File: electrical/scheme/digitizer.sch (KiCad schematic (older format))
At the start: 149 parts, among them P1 mode, P10 in-2, P11 in-3, P12 in-1, P13 USB_B, P2 ~rst~, P3 ext, P4 trig, P5 trig-mode, P6 swd, P7 out-0, P8 out-1, P9 in-0, U1 AD8672, U10 crystal-4pin, U100 AD8672, U101 AD8672, U11 CP2102, U12 adr4533, U13 BAT54S, U14 adr4533, U15 ADT7410, U16 MCP1703T-3302E/CB, U17 AD7683, U18 NCP3063, U19 ADG5204, U2 AD8672, U20 NCP3063, U3 AD8672

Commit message: a
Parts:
- added R77, R78: 1k 5%, Resistors_SMD:R_0805_HandSoldering, symbol R
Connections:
- wire segments 542 -> 544
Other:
- moved on the sheet: P7, P8
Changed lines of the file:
@@
 L BNC P7
 U 1 1 55AB2116
-P 24400 7650
-F 0 "P7" H 24410 7770 50  0000 C CNN
-F 1 "out-0" V 24510 7590 50  0000 C CNN
-F 2 "Sockets_BNC:BNC_Socket_TYCO-AMP_LargePads" H 24400 7650 60  0001 C CNN
-F 3 "" H 24400 7650 60  0000 C CNN
-	1    24400 7650
+P 24900 7650
+F 0 "P7" H 24910 7770 50  0000 C CNN
+F 1 "out-0" V 25010 7590 50  0000 C CNN
+F 2 "Sockets_BNC:BNC_Socket_TYCO-AMP_LargePads" H 24900 7650 60  0001 C CNN
+F 3 "" H 24900 7650 60  0000 C CNN
+	1    24900 7650
 	1    0    0    -1
 $EndComp
@@
 L GNDA #PWR075
 U 1 1 55AB5E7E
-P 24400 7950
-F 0 "#PWR075" H 24400 7700 50  0001 C CNN
-F 1 "GNDA" H 24400 7800 50  0000 C CNN
-F 2 "" H 24400 7950 60  0000 C CNN
-F 3 "" H 24400 7950 60  0000 C CNN
-	1    24400 7950
+P 24900 7950
+F 0 "#PWR075" H 24900 7700 50  0001 C CNN
+F 1 "GNDA" H 24900 7800 50  0000 C CNN
+F 2 "" H 24900 7950 60  0000 C CNN
+F 3 "" H 24900 7950 60  0000 C CNN
+	1    24900 7950
 	1    0    0    -1
 $EndComp
@@
 L BNC P8
 U 1 1 55ABA9EF
-P 24450 11850
-F 0 "P8" H 24460 11970 50  0000 C CNN
-F 1 "out-1" V 24560 11790 50  0000 C CNN
-F 2 "Sockets_BNC:BNC_Socket_TYCO-AMP_LargePads" H 24450 11850 60  0001 C CNN
-F 3 "" H 24450 11850 60  0000 C CNN
-	1    24450 11850
+P 24950 11850
+F 0 "P8" H 24960 11970 50  0000 C CNN
+F 1 "out-1" V 25060 11790 50  0000 C CNN
+F 2 "Sockets_BNC:BNC_Socket_TYCO-AMP_LargePads" H 24950 11850 60  0001 C CNN
+F 3 "" H 24950 11850 60  0000 C CNN
+	1    24950 11850
 	1    0    0    -1
 $EndComp
@@
 L GNDA #PWR076
 U 1 1 55ABA9F6
-P 24450 12150
-F 0 "#PWR076" H 24450 11900 50  0001 C CNN
-F 1 "GNDA" H 24450 12000 50  0000 C CNN
-F 2 "" H 24450 12150 60  0000 C CNN
-F 3 "" H 24450 12150 60  0000 C CNN
-	1    24450 12150
+P 24950 12150
+F 0 "#PWR076" H 24950 11900 50  0001 C CNN
+F 1 "GNDA" H 24950 12000 50  0000 C CNN
+F 2 "" H 24950 12150 60  0000 C CNN
+F 3 "" H 24950 12150 60  0000 C CNN
+	1    24950 12150
 	1    0    0    -1
 $EndComp
@@
 	1700 12200 1700 12450
 Wire Wire Line
-	24400 7850 24400 7950
-Wire Wire Line
-	24450 12050 24450 12150
+	24900 7850 24900 7950
+Wire Wire Line
+	24950 12050 24950 12150
 Wire Wire Line
 	9150 3000 10000 3000
@@
 Text Label 11500 15750 0    60   ~ 0
 i2c1-sda
+$Comp
+L R R77
+U 1 1 55B37111
+P 24400 7650
+F 0 "R77" V 24480 7650 50  0000 C CNN
+F 1 "1k 5%" V 24400 7650 50  0000 C CNN
+F 2 "Resistors_SMD:R_0805_HandSoldering" V 24330 7650 30  0001 C CNN
+F 3 "" H 24400 7650 30  0000 C CNN
+	1    24400 7650
+	0    -1   -1   0
+$EndComp
+Wire Wire Line
+	24750 7650 24550 7650
+$Comp
+L R R78
+U 1 1 55B3C1AC
+P 24450 11850
+F 0 "R78" V 24530 11850 50  0000 C CNN
+F 1 "1k 5%" V 24450 11850 50  0000 C CNN
+F 2 "Resistors_SMD:R_0805_HandSoldering" V 24380 11850 30  0001 C CNN
+F 3 "" H 24450 11850 30  0000 C CNN
+	1    24450 11850
+	0    -1   -1   0
+$EndComp
+Wire Wire Line
+	24800 11850 24600 11850
 $EndSCHEMATC

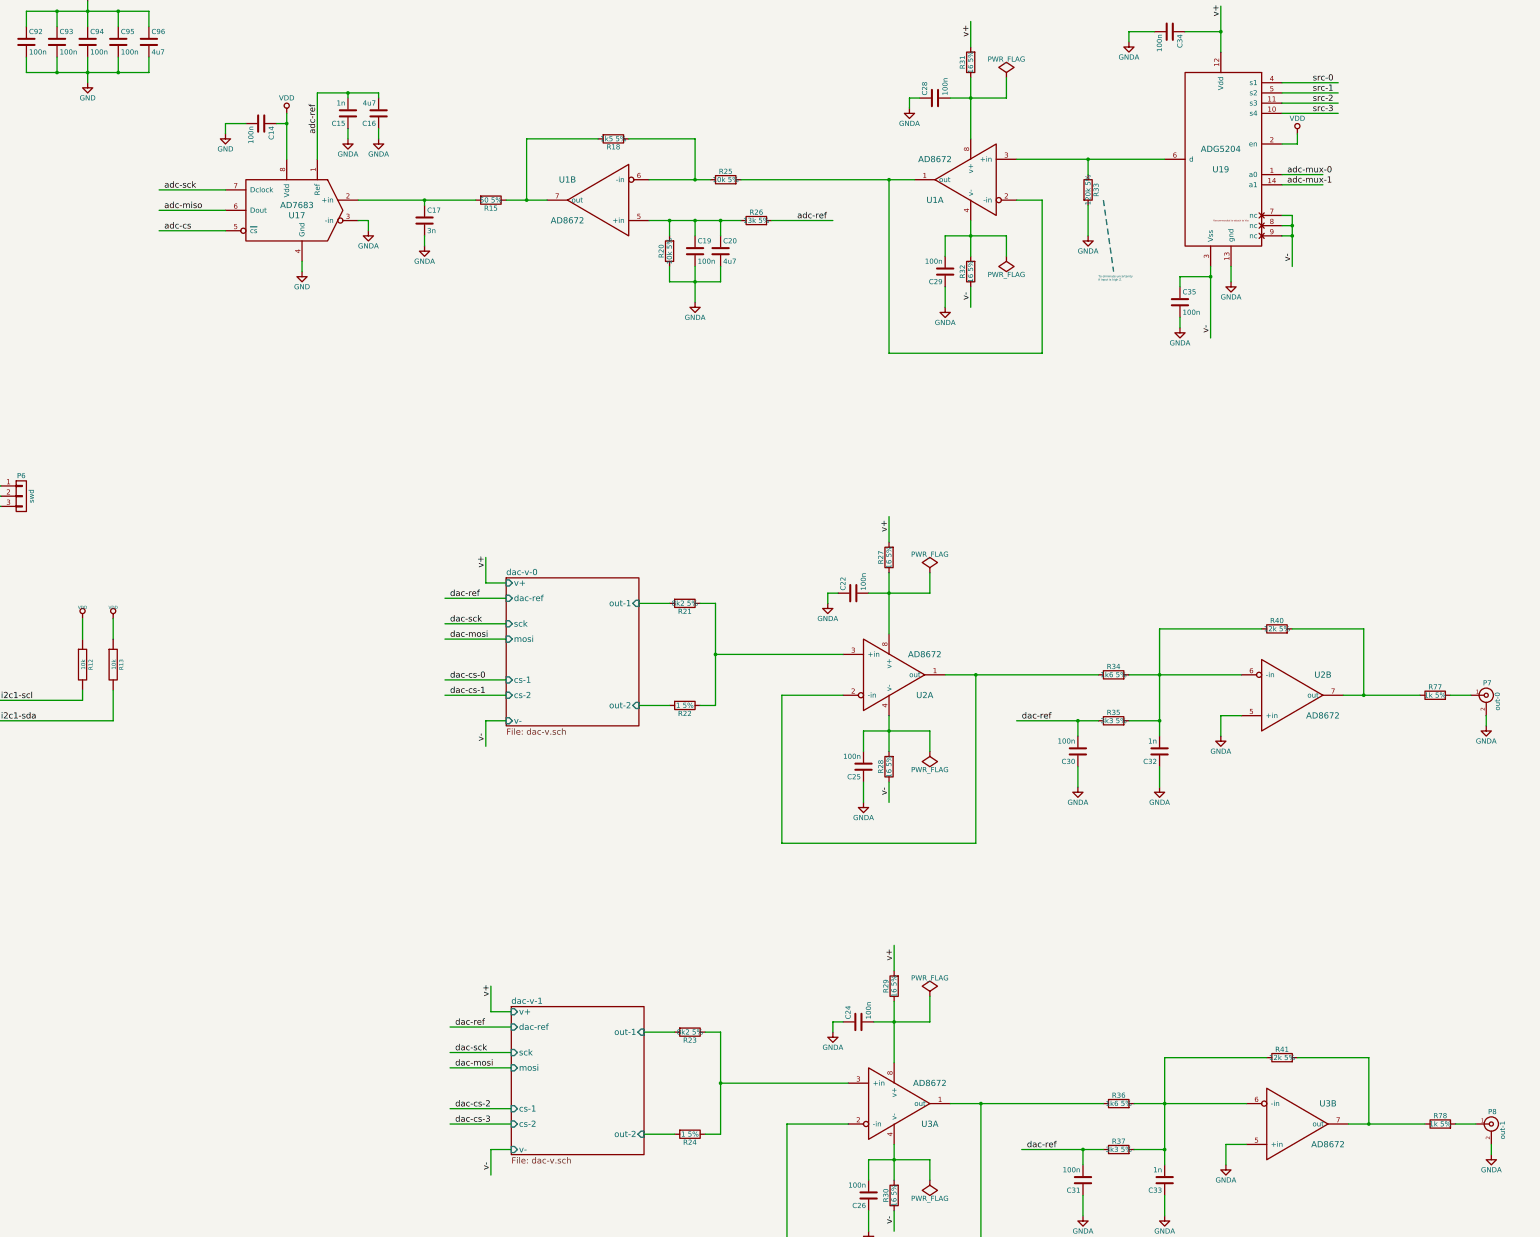
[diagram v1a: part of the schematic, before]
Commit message: Added capacitors for making opamp driving capacitive load stable.
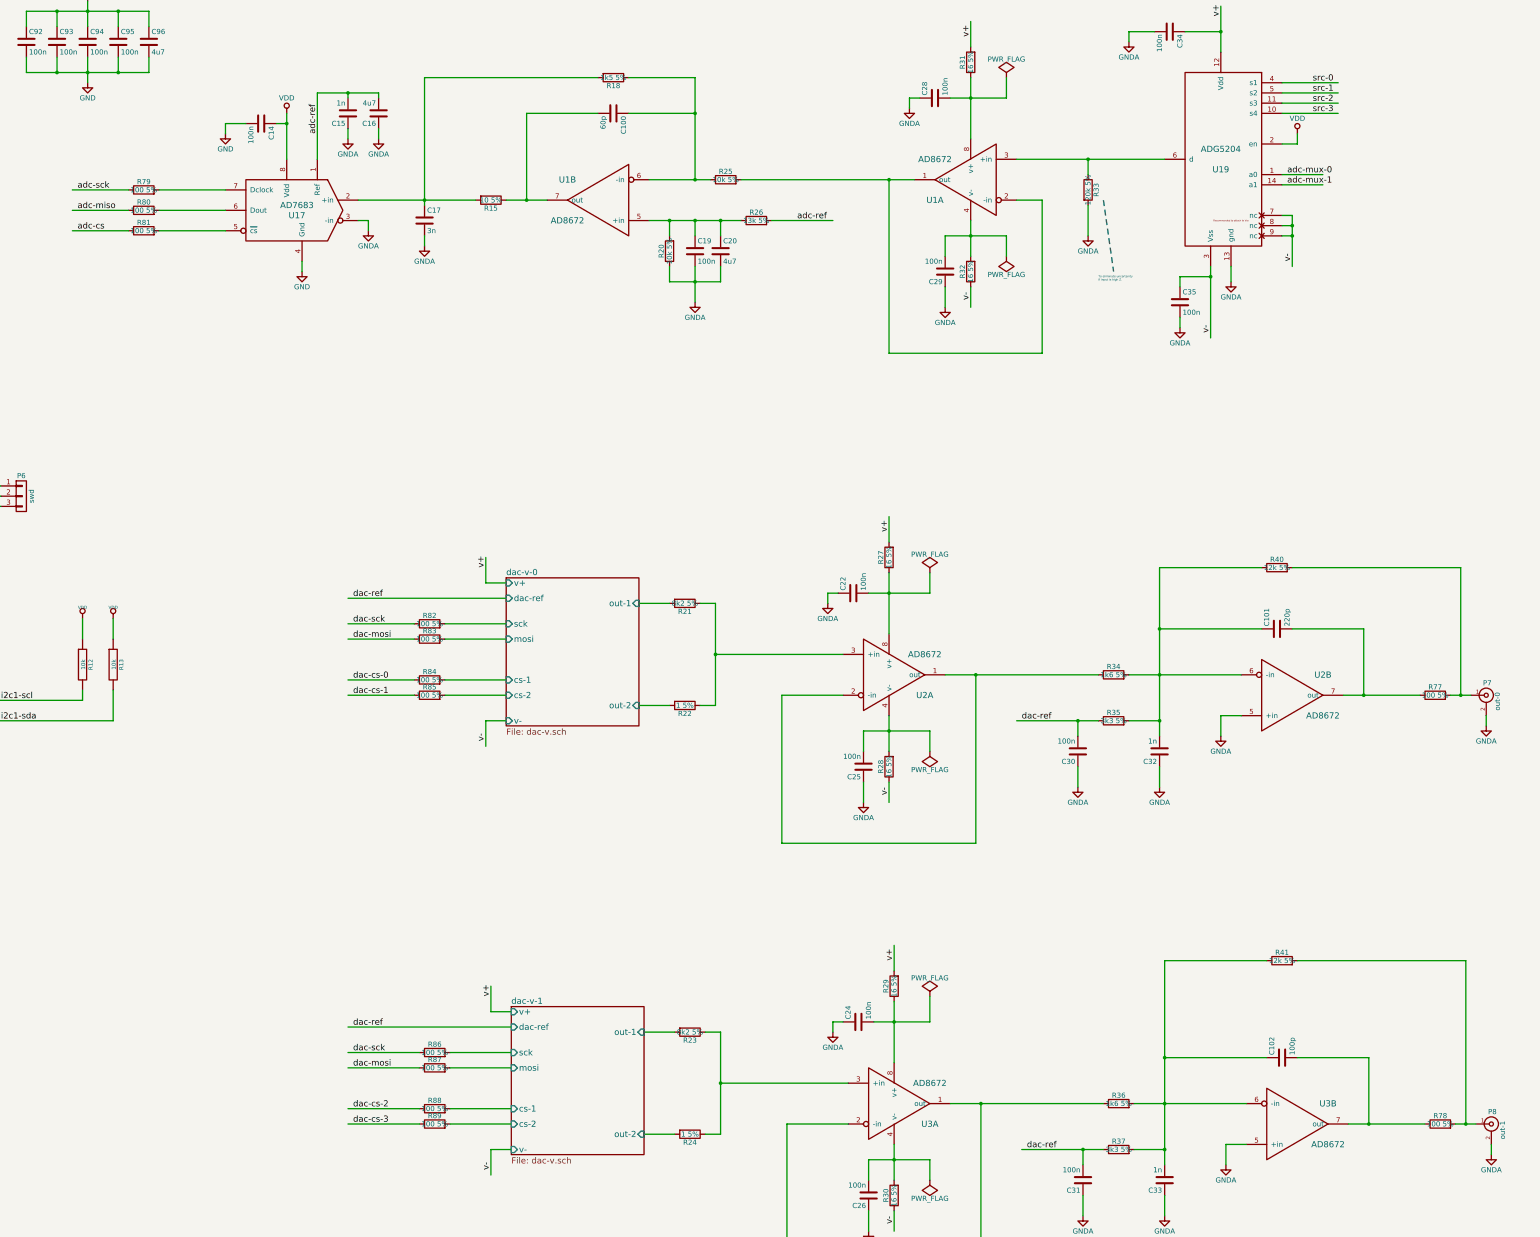
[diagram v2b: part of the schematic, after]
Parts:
- added C100: 60p, Capacitors_SMD:C_0805_HandSoldering, symbol C
- added C101: 220p, Capacitors_SMD:C_0805_HandSoldering, symbol C
- added C102: 100p, Capacitors_SMD:C_0805_HandSoldering, symbol C
- added R79, R80, R81, R82, R83, R84, R85, R86, R87, R88, R89: 100 5%, Resistors_SMD:R_0805_HandSoldering, symbol R
- R15: value 50 5% -> 10 5%
- R77, R78: value 1k 5% -> 100 5%
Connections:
- wire segments 544 -> 563
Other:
- moved on the sheet: R18, R40, R41

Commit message: a
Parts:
- added R90, R91, R92, R93: 1k 5%, Resistors_SMD:R_0805_HandSoldering, symbol R
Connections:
- wire segments 563 -> 567
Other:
- moved on the sheet: P10, P11, P12, P9
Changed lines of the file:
@@
 L BNC P9
 U 1 1 559CB400
-P 30950 3300
-F 0 "P9" H 30960 3420 50  0000 C CNN
-F 1 "in-0" V 31060 3240 50  0000 C CNN
-F 2 "Sockets_BNC:BNC_Socket_TYCO-AMP_LargePads" H 30950 3300 60  0001 C CNN
-F 3 "" H 30950 3300 60  0000 C CNN
-	1    30950 3300
+P 31450 3300
+F 0 "P9" H 31460 3420 50  0000 C CNN
+F 1 "in-0" V 31560 3240 50  0000 C CNN
+F 2 "Sockets_BNC:BNC_Socket_TYCO-AMP_LargePads" H 31450 3300 60  0001 C CNN
+F 3 "" H 31450 3300 60  0000 C CNN
+	1    31450 3300
 	1    0    0    -1
 $EndComp
@@
 L GNDA #PWR058
 U 1 1 559CD9D7
-P 30950 3600
-F 0 "#PWR058" H 30950 3350 50  0001 C CNN
-F 1 "GNDA" H 30950 3450 50  0000 C CNN
-F 2 "" H 30950 3600 60  0000 C CNN
-F 3 "" H 30950 3600 60  0000 C CNN
-	1    30950 3600
+P 31450 3600
+F 0 "#PWR058" H 31450 3350 50  0001 C CNN
+F 1 "GNDA" H 31450 3450 50  0000 C CNN
+F 2 "" H 31450 3600 60  0000 C CNN
+F 3 "" H 31450 3600 60  0000 C CNN
+	1    31450 3600
 	1    0    0    -1
 $EndComp
@@
 L BNC P10
 U 1 1 55BF1FCC
-P 30900 9350
-F 0 "P10" H 30910 9470 50  0000 C CNN
-F 1 "in-2" V 31010 9290 50  0000 C CNN
-F 2 "Sockets_BNC:BNC_Socket_TYCO-AMP_LargePads" H 30900 9350 60  0001 C CNN
-F 3 "" H 30900 9350 60  0000 C CNN
-	1    30900 9350
+P 31400 9350
+F 0 "P10" H 31410 9470 50  0000 C CNN
+F 1 "in-2" V 31510 9290 50  0000 C CNN
+F 2 "Sockets_BNC:BNC_Socket_TYCO-AMP_LargePads" H 31400 9350 60  0001 C CNN
+F 3 "" H 31400 9350 60  0000 C CNN
+	1    31400 9350
 	1    0    0    -1
 $EndComp
@@
 L GNDA #PWR0100
 U 1 1 55BF1FD3
-P 30900 9650
-F 0 "#PWR0100" H 30900 9400 50  0001 C CNN
-F 1 "GNDA" H 30900 9500 50  0000 C CNN
-F 2 "" H 30900 9650 60  0000 C CNN
-F 3 "" H 30900 9650 60  0000 C CNN
-	1    30900 9650
+P 31400 9650
+F 0 "#PWR0100" H 31400 9400 50  0001 C CNN
+F 1 "GNDA" H 31400 9500 50  0000 C CNN
+F 2 "" H 31400 9650 60  0000 C CNN
+F 3 "" H 31400 9650 60  0000 C CNN
+	1    31400 9650
 	1    0    0    -1
 $EndComp
@@
 L BNC P12
 U 1 1 55BF7CDF
-P 30950 5950
-F 0 "P12" H 30960 6070 50  0000 C CNN
-F 1 "in-1" V 31060 5890 50  0000 C CNN
-F 2 "Sockets_BNC:BNC_Socket_TYCO-AMP_LargePads" H 30950 5950 60  0001 C CNN
-F 3 "" H 30950 5950 60  0000 C CNN
-	1    30950 5950
+P 31450 5950
+F 0 "P12" H 31460 6070 50  0000 C CNN
+F 1 "in-1" V 31560 5890 50  0000 C CNN
+F 2 "Sockets_BNC:BNC_Socket_TYCO-AMP_LargePads" H 31450 5950 60  0001 C CNN
+F 3 "" H 31450 5950 60  0000 C CNN
+	1    31450 5950
 	1    0    0    -1
 $EndComp
@@
 L GNDA #PWR0105
 U 1 1 55BF7CE6
-P 30950 6250
-F 0 "#PWR0105" H 30950 6000 50  0001 C CNN
-F 1 "GNDA" H 30950 6100 50  0000 C CNN
-F 2 "" H 30950 6250 60  0000 C CNN
-F 3 "" H 30950 6250 60  0000 C CNN
-	1    30950 6250
+P 31450 6250
+F 0 "#PWR0105" H 31450 6000 50  0001 C CNN
+F 1 "GNDA" H 31450 6100 50  0000 C CNN
+F 2 "" H 31450 6250 60  0000 C CNN
+F 3 "" H 31450 6250 60  0000 C CNN
+	1    31450 6250
 	1    0    0    -1
 $EndComp
@@
 L BNC P11
 U 1 1 55BFAAD0
-P 30900 12150
-F 0 "P11" H 30910 12270 50  0000 C CNN
-F 1 "in-3" V 31010 12090 50  0000 C CNN
-F 2 "Sockets_BNC:BNC_Socket_TYCO-AMP_LargePads" H 30900 12150 60  0001 C CNN
-F 3 "" H 30900 12150 60  0000 C CNN
-	1    30900 12150
+P 31400 12150
+F 0 "P11" H 31410 12270 50  0000 C CNN
+F 1 "in-3" V 31510 12090 50  0000 C CNN
+F 2 "Sockets_BNC:BNC_Socket_TYCO-AMP_LargePads" H 31400 12150 60  0001 C CNN
+F 3 "" H 31400 12150 60  0000 C CNN
+	1    31400 12150
 	1    0    0    -1
 $EndComp
@@
 L GNDA #PWR0106
 U 1 1 55BFAAD7
-P 30900 12450
-F 0 "#PWR0106" H 30900 12200 50  0001 C CNN
-F 1 "GNDA" H 30900 12300 50  0000 C CNN
-F 2 "" H 30900 12450 60  0000 C CNN
-F 3 "" H 30900 12450 60  0000 C CNN
-	1    30900 12450
+P 31400 12450
+F 0 "#PWR0106" H 31400 12200 50  0001 C CNN
+F 1 "GNDA" H 31400 12300 50  0000 C CNN
+F 2 "" H 31400 12450 60  0000 C CNN
+F 3 "" H 31400 12450 60  0000 C CNN
+	1    31400 12450
 	1    0    0    -1
 $EndComp
@@
 	21150 2800 21250 3500
 Wire Wire Line
-	30950 3500 30950 3600
+	31450 3500 31450 3600
 Wire Wire Line
 	9150 15150 9850 15150
@@
 	28900 9150 29400 9150
 Wire Wire Line
-	30900 9550 30900 9650
+	31400 9550 31400 9650
 Wire Wire Line
 	30400 9350 30750 9350
@@
 Connection ~ 29300 5750
 Wire Wire Line
-	30950 6150 30950 6250
+	31450 6150 31450 6250
 Wire Wire Line
 	29350 11950 28900 11950
@@
 Connection ~ 29250 11950
 Wire Wire Line
-	30900 12350 30900 12450
+	31400 12350 31400 12450
 Wire Wire Line
 	5700 20850 6500 20850
@@
 	15500 1950 15500 2800
 Connection ~ 15500 2800
+$Comp
+L R R92
+U 1 1 55BD770F
+P 30950 3300
+F 0 "R92" V 31030 3300 50  0000 C CNN
+F 1 "1k 5%" V 30950 3300 50  0000 C CNN
+F 2 "Resistors_SMD:R_0805_HandSoldering" V 30880 3300 30  0001 C CNN
+F 3 "" H 30950 3300 30  0000 C CNN
+	1    30950 3300
+	0    1    1    0
+$EndComp
+Wire Wire Line
+	31100 3300 31300 3300
+$Comp
+L R R93
+U 1 1 55BDE631
+P 30950 5950
+F 0 "R93" V 31030 5950 50  0000 C CNN
+F 1 "1k 5%" V 30950 5950 50  0000 C CNN
+F 2 "Resistors_SMD:R_0805_HandSoldering" V 30880 5950 30  0001 C CNN
+F 3 "" H 30950 5950 30  0000 C CNN
+	1    30950 5950
+	0    1    1    0
+$EndComp
+Wire Wire Line
+	31100 5950 31300 5950
+$Comp
+L R R90
+U 1 1 55BE0CA7
+P 30900 9350
+F 0 "R90" V 30980 9350 50  0000 C CNN
+F 1 "1k 5%" V 30900 9350 50  0000 C CNN
+F 2 "Resistors_SMD:R_0805_HandSoldering" V 30830 9350 30  0001 C CNN
+F 3 "" H 30900 9350 30  0000 C CNN
+	1    30900 9350
+	0    1    1    0
+$EndComp
+Wire Wire Line
+	31250 9350 31050 9350
+$Comp
+L R R91
+U 1 1 55BE6200
+P 30900 12150
+F 0 "R91" V 30980 12150 50  0000 C CNN
+F 1 "1k 5%" V 30900 12150 50  0000 C CNN
+F 2 "Resistors_SMD:R_0805_HandSoldering" V 30830 12150 30  0001 C CNN
+F 3 "" H 30900 12150 30  0000 C CNN
+	1    30900 12150
+	0    1    1    0
+$EndComp
+Wire Wire Line
+	31050 12150 31250 12150
 $EndSCHEMATC

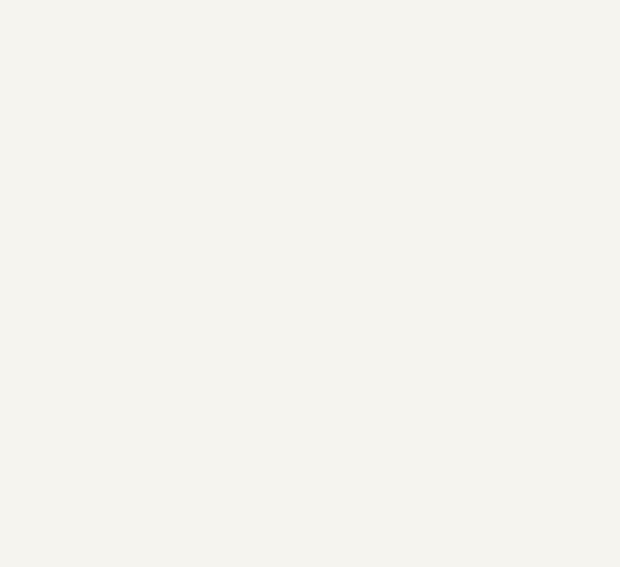
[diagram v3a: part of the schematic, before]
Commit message: Inserted holding screw holes.
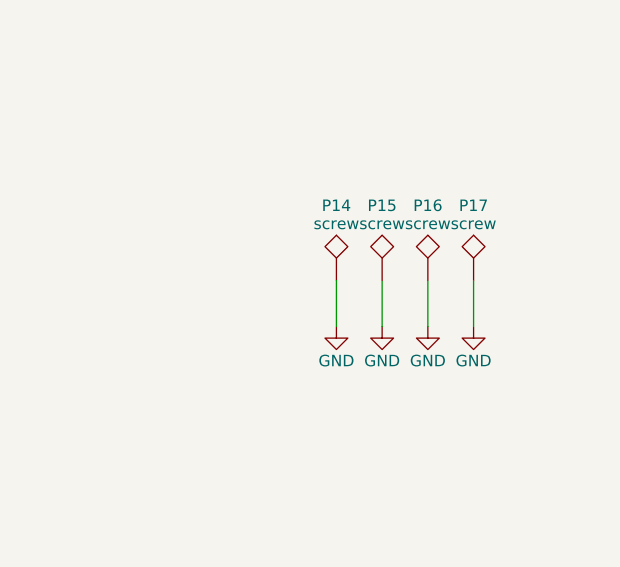
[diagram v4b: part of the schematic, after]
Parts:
- added P14, P15, P16, P17: screw, Divers:douille_4mm, symbol TST
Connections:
- wire segments 567 -> 571
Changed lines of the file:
@@
 Wire Wire Line
 	31050 12150 31250 12150
+$Comp
+L TST P14
+U 1 1 55C19FBA
+P 30450 15350
+F 0 "P14" H 30450 15650 50  0000 C BNN
+F 1 "screw" H 30450 15600 50  0000 C CNN
+F 2 "Divers:douille_4mm" H 30450 15350 60  0001 C CNN
+F 3 "" H 30450 15350 60  0000 C CNN
+	1    30450 15350
+	1    0    0    -1
+$EndComp
+Wire Wire Line
+	30450 15350 30450 15550
+$Comp
+L GND #PWR0131
+U 1 1 55C1E9F0
+P 30450 15550
+F 0 "#PWR0131" H 30450 15300 50  0001 C CNN
+F 1 "GND" H 30450 15400 50  0000 C CNN
+F 2 "" H 30450 15550 60  0000 C CNN
+F 3 "" H 30450 15550 60  0000 C CNN
+	1    30450 15550
+	1    0    0    -1
+$EndComp
+$Comp
+L TST P15
+U 1 1 55C1EC41
+P 30650 15350
+F 0 "P15" H 30650 15650 50  0000 C BNN
+F 1 "screw" H 30650 15600 50  0000 C CNN
+F 2 "Divers:douille_4mm" H 30650 15350 60  0001 C CNN
+F 3 "" H 30650 15350 60  0000 C CNN
+	1    30650 15350
+	1    0    0    -1
+$EndComp
+Wire Wire Line
+	30650 15350 30650 15550
+$Comp
+L GND #PWR0132
+U 1 1 55C1EC48
+P 30650 15550
+F 0 "#PWR0132" H 30650 15300 50  0001 C CNN
+F 1 "GND" H 30650 15400 50  0000 C CNN
+F 2 "" H 30650 15550 60  0000 C CNN
+F 3 "" H 30650 15550 60  0000 C CNN
+	1    30650 15550
+	1    0    0    -1
+$EndComp
+$Comp
+L TST P16
+U 1 1 55C1EE9C
+P 30850 15350
+F 0 "P16" H 30850 15650 50  0000 C BNN
+F 1 "screw" H 30850 15600 50  0000 C CNN
+F 2 "Divers:douille_4mm" H 30850 15350 60  0001 C CNN
+F 3 "" H 30850 15350 60  0000 C CNN
+	1    30850 15350
+	1    0    0    -1
+$EndComp
+Wire Wire Line
+	30850 15350 30850 15550
+$Comp
+L GND #PWR0133
+U 1 1 55C1EEA3
+P 30850 15550
+F 0 "#PWR0133" H 30850 15300 50  0001 C CNN
+F 1 "GND" H 30850 15400 50  0000 C CNN
+F 2 "" H 30850 15550 60  0000 C CNN
+F 3 "" H 30850 15550 60  0000 C CNN
+	1    30850 15550
+	1    0    0    -1
+$EndComp
+$Comp
+L TST P17
+U 1 1 55C1EEA9
+P 31050 15350
+F 0 "P17" H 31050 15650 50  0000 C BNN
+F 1 "screw" H 31050 15600 50  0000 C CNN
+F 2 "Divers:douille_4mm" H 31050 15350 60  0001 C CNN
+F 3 "" H 31050 15350 60  0000 C CNN
+	1    31050 15350
+	1    0    0    -1
+$EndComp
+Wire Wire Line
+	31050 15350 31050 15550
+$Comp
+L GND #PWR0134
+U 1 1 55C1EEB0
+P 31050 15550
+F 0 "#PWR0134" H 31050 15300 50  0001 C CNN
+F 1 "GND" H 31050 15400 50  0000 C CNN
+F 2 "" H 31050 15550 60  0000 C CNN
+F 3 "" H 31050 15550 60  0000 C CNN
+	1    31050 15550
+	1    0    0    -1
+$EndComp
 $EndSCHEMATC

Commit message: a
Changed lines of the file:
@@
 Text Label 23200 1750 0    60   ~ 0
 src-1
+Text Label 23200 1950 0    60   ~ 0
+src-2
 Text Label 23200 1850 0    60   ~ 0
-src-2
-Text Label 23200 1950 0    60   ~ 0
 src-3
 $Comp

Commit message: a
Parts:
- added R94, R95: 100 5%, Resistors_SMD:R_0805_HandSoldering, symbol R
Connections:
- wire segments 571 -> 573
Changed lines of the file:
@@
 	1    0    0    -1
 $EndComp
-Text Label 22950 2550 0    60   ~ 0
+Text Label 23850 2550 0    60   ~ 0
 adc-mux-0
-Text Label 22950 2650 0    60   ~ 0
+Text Label 23850 2650 0    60   ~ 0
 adc-mux-1
 $Comp
@@
 	1    0    0    -1
 $EndComp
+$Comp
+L R R94
+U 1 1 55A94CE2
+P 23450 2550
+F 0 "R94" V 23530 2550 50  0000 C CNN
+F 1 "100 5%" V 23450 2550 50  0000 C CNN
+F 2 "Resistors_SMD:R_0805_HandSoldering" V 23380 2550 30  0001 C CNN
+F 3 "" H 23450 2550 30  0000 C CNN
+	1    23450 2550
+	0    -1   -1   0
+$EndComp
+$Comp
+L R R95
+U 1 1 55A9753A
+P 23450 2650
+F 0 "R95" V 23530 2650 50  0000 C CNN
+F 1 "100 5%" V 23450 2650 50  0000 C CNN
+F 2 "Resistors_SMD:R_0805_HandSoldering" V 23380 2650 30  0001 C CNN
+F 3 "" H 23450 2650 30  0000 C CNN
+	1    23450 2650
+	0    -1   -1   0
+$EndComp
+Wire Wire Line
+	23600 2550 24400 2550
+Wire Wire Line
+	23600 2650 24400 2650
 $EndSCHEMATC
